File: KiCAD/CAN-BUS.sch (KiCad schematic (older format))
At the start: 11 parts

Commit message: Schematic Rev 0
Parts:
- C16, C18: renamed from C?; value TBD -> 22pF
- gave numbers to parts that had none: 9
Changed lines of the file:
@@
 LIBS:mcp2551
 LIBS:cesd5v0ap
+LIBS:usb_micro_b
 LIBS:Pressure Scanner Board-cache
 EELAYER 25 0
@@
 CAN Controller + Transceiver
 $Comp
-L MCP2515 U?
+L MCP2515 U14
 U 1 1 5C6487A3
 P 4150 3800
-F 0 "U?" H 4150 3175 49  0000 C CNN
+F 0 "U14" H 4150 3175 49  0000 C CNN
 F 1 "MCP2515" H 4150 4500 49  0000 C CNN
 F 2 "" H 2950 3675 49  0001 C CNN
@@
 $EndComp
 $Comp
-L MCP2551 U?
+L MCP2551 U13
 U 1 1 5C6487CB
 P 7600 3775
-F 0 "U?" H 7600 3450 49  0000 C CNN
+F 0 "U13" H 7600 3450 49  0000 C CNN
 F 1 "MCP2551" H 7600 4100 49  0000 C CNN
 F 2 "" H 7600 3775 49  0001 C CNN
@@
 RXCAN
 $Comp
-L GND #PWR?
+L GND #PWR62
 U 1 1 5C648816
 P 3425 4350
-F 0 "#PWR?" H 3425 4100 50  0001 C CNN
+F 0 "#PWR62" H 3425 4100 50  0001 C CNN
 F 1 "GND" H 3425 4200 50  0000 C CNN
 F 2 "" H 3425 4350 50  0001 C CNN
@@
 	3425 4275 3550 4275
 $Comp
-L +3.3V #PWR?
+L +3.3V #PWR55
 U 1 1 5C6489C6
 P 4875 2900
-F 0 "#PWR?" H 4875 2750 50  0001 C CNN
+F 0 "#PWR55" H 4875 2750 50  0001 C CNN
 F 1 "+3.3V" H 4875 3040 50  0000 C CNN
 F 2 "" H 4875 2900 50  0001 C CNN
@@
 NoConn ~ 4750 4275
 $Comp
-L R_Small R?
+L R_Small R10
 U 1 1 5C648A47
 P 5050 3125
-F 0 "R?" H 5080 3145 50  0000 L CNN
+F 0 "R10" H 5080 3145 50  0000 L CNN
 F 1 "10K" H 5080 3085 50  0000 L CNN
 F 2 "" H 5050 3125 50  0001 C CNN
@@
 	5050 4025 4750 4025
 $Comp
-L Crystal Y?
+L Crystal Y2
 U 1 1 5C648B55
 P 2850 4100
-F 0 "Y?" V 2900 4275 50  0000 C CNN
+F 0 "Y2" V 2900 4275 50  0000 C CNN
 F 1 "16MHz" V 2850 3850 50  0000 C CNN
 F 2 "" H 2850 4100 50  0001 C CNN
@@
 	3150 4150 3550 4150
 $Comp
-L C_Small C?
+L C_Small C16
 U 1 1 5C648C45
 P 2325 3900
-F 0 "C?" H 2335 3970 50  0000 L CNN
-F 1 "TBD" H 2335 3820 50  0000 L CNN
+F 0 "C16" V 2425 3925 50  0000 L CNN
+F 1 "22pF" V 2200 3825 50  0000 L CNN
 F 2 "" H 2325 3900 50  0001 C CNN
 F 3 "" H 2325 3900 50  0001 C CNN
@@
 $EndComp
 $Comp
-L C_Small C?
+L C_Small C18
 U 1 1 5C648C82
 P 2325 4300
-F 0 "C?" H 2335 4370 50  0000 L CNN
-F 1 "TBD" H 2335 4220 50  0000 L CNN
+F 0 "C18" V 2200 4200 50  0000 L CNN
+F 1 "22pF" V 2425 4200 50  0000 L CNN
 F 2 "" H 2325 4300 50  0001 C CNN
 F 3 "" H 2325 4300 50  0001 C CNN
@@
 $EndComp
 $Comp
-L GND #PWR?
+L GND #PWR60
 U 1 1 5C648CB1
 P 2050 4100
-F 0 "#PWR?" H 2050 3850 50  0001 C CNN
+F 0 "#PWR60" H 2050 3850 50  0001 C CNN
 F 1 "GND" H 2050 3950 50  0000 C CNN
 F 2 "" H 2050 4100 50  0001 C CNN
@@
 	6975 3575 7125 3575
 $Comp
-L GND #PWR?
+L GND #PWR59
 U 1 1 5C649298
 P 6975 3700
-F 0 "#PWR?" H 6975 3450 50  0001 C CNN
+F 0 "#PWR59" H 6975 3450 50  0001 C CNN
 F 1 "GND" H 6975 3550 50  0000 C CNN
 F 2 "" H 6975 3700 50  0001 C CNN
@@
 	6975 3700 7125 3700
 $Comp
-L +5V #PWR?
+L +5V #PWR58
 U 1 1 5C6492E1
 P 6500 3675
-F 0 "#PWR?" H 6500 3525 50  0001 C CNN
+F 0 "#PWR58" H 6500 3525 50  0001 C CNN
 F 1 "+5V" H 6500 3815 50  0000 C CNN
 F 2 "" H 6500 3675 50  0001 C CNN
@@
 	6500 3825 7125 3825
 $Comp
-L R_Small R?
+L R_Small R11
 U 1 1 5C64939D
 P 8250 3575
-F 0 "R?" V 8400 3550 50  0000 L CNN
+F 0 "R11" V 8400 3550 50  0000 L CNN
 F 1 "17K" V 8325 3500 50  0000 L CNN
 F 2 "" H 8250 3575 50  0001 C CNN
@@
 $EndComp
 $Comp
-L GND #PWR?
+L GND #PWR57
 U 1 1 5C649485
 P 8450 3575
-F 0 "#PWR?" H 8450 3325 50  0001 C CNN
+F 0 "#PWR57" H 8450 3325 50  0001 C CNN
 F 1 "GND" H 8450 3425 50  0000 C CNN
 F 2 "" H 8450 3575 50  0001 C CNN
@@
 NoConn ~ 8075 3950
 $Comp
-L CESD5V0AP D?
+L CESD5V0AP D5
 U 1 1 5C649B06
 P 8400 4275
-F 0 "D?" H 8600 4335 39  0000 C CNN
+F 0 "D5" H 8600 4335 39  0000 C CNN
 F 1 "CESD5V0AP" H 8725 4390 39  0000 C CNN
 F 2 "" H 8400 4275 39  0001 C CNN
@@
 $EndComp
 $Comp
-L GND #PWR?
+L GND #PWR63
 U 1 1 5C649B47
 P 8400 4550
-F 0 "#PWR?" H 8400 4300 50  0001 C CNN
+F 0 "#PWR63" H 8400 4300 50  0001 C CNN
 F 1 "GND" H 8400 4400 50  0000 C CNN
 F 2 "" H 8400 4550 50  0001 C CNN
@@
 	8480 3700 8075 3700
 $Comp
-L R R?
+L R R12
 U 1 1 5C649D1F
 P 9175 3750
-F 0 "R?" V 9255 3750 50  0000 C CNN
+F 0 "R12" V 9255 3750 50  0000 C CNN
 F 1 "120" V 9175 3750 50  0000 C CNN
 F 2 "" V 9105 3750 50  0001 C CNN
@@
 Transient Voltage Protection
 $Comp
-L C_Small C?
+L C_Small C17
 U 1 1 5C64AAF4
 P 6500 3975
-F 0 "C?" H 6400 4050 50  0000 L CNN
+F 0 "C17" H 6400 4050 50  0000 L CNN
 F 1 "100nF" H 6250 3900 50  0000 L CNN
 F 2 "" H 6500 3975 50  0001 C CNN
@@
 $EndComp
 $Comp
-L GND #PWR?
+L GND #PWR61
 U 1 1 5C64ABB3
 P 6500 4125
-F 0 "#PWR?" H 6500 3875 50  0001 C CNN
+F 0 "#PWR61" H 6500 3875 50  0001 C CNN
 F 1 "GND" H 6500 3975 50  0000 C CNN
 F 2 "" H 6500 4125 50  0001 C CNN
@@
 Connection ~ 6500 3825
 $Comp
-L C_Small C?
+L C_Small C15
 U 1 1 5C64AE69
 P 5300 3125
-F 0 "C?" H 5310 3195 50  0000 L CNN
+F 0 "C15" H 5310 3195 50  0000 L CNN
 F 1 "100nF" H 5310 3045 50  0000 L CNN
 F 2 "" H 5300 3125 50  0001 C CNN
@@
 Connection ~ 5050 2950
 $Comp
-L GND #PWR?
+L GND #PWR56
 U 1 1 5C64B180
 P 5300 3275
-F 0 "#PWR?" H 5300 3025 50  0001 C CNN
+F 0 "#PWR56" H 5300 3025 50  0001 C CNN
 F 1 "GND" H 5300 3125 50  0000 C CNN
 F 2 "" H 5300 3275 50  0001 C CNN

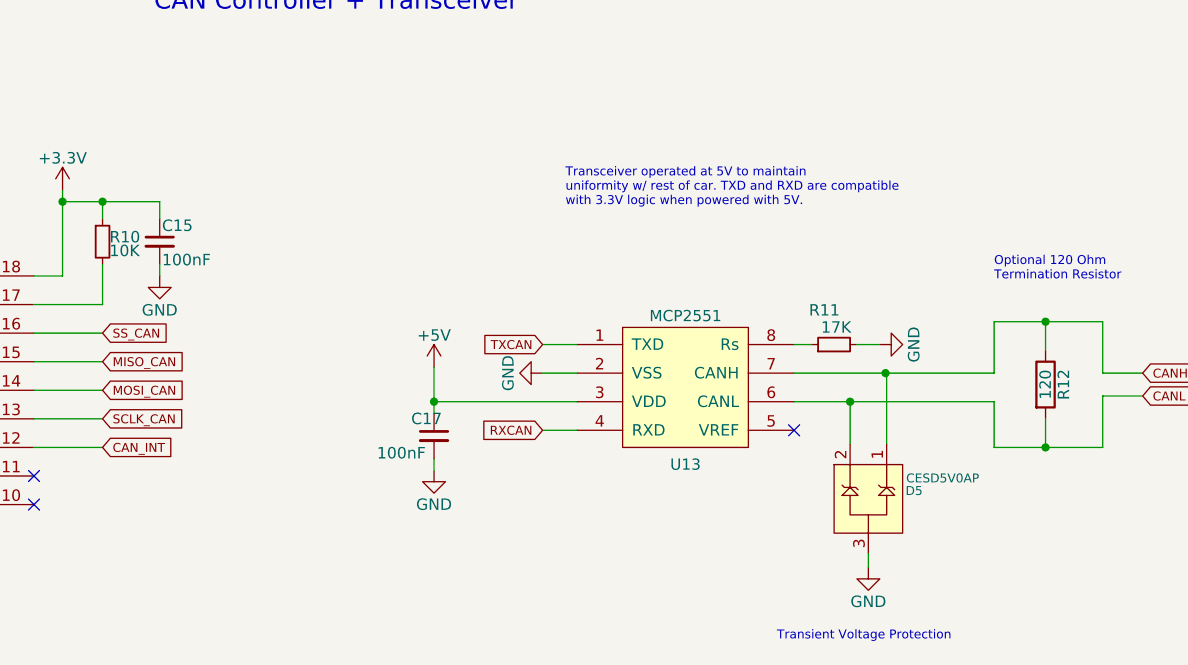
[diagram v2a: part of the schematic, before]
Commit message: Added footprints for all components and created BOM
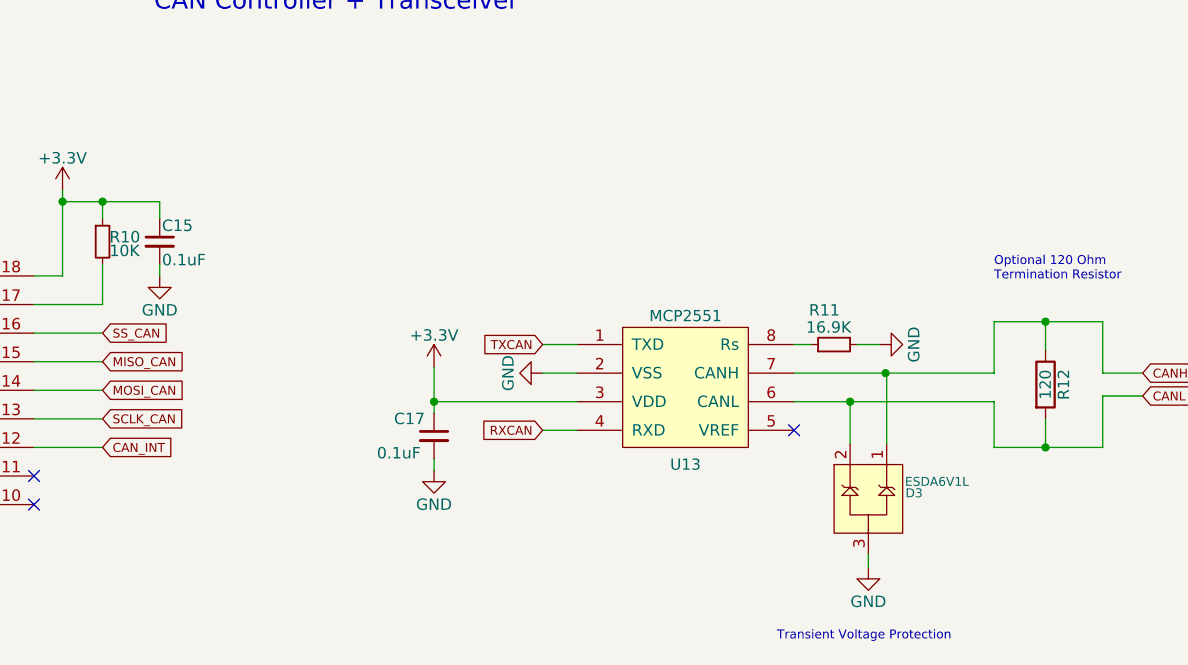
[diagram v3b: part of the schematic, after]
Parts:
- removed D5: CESD5V0AP, symbol CESD5V0AP
- added D3: ESDA6V1L, TO_SOT_Packages_SMD:SOT-23, symbol ESDA6V1L
- C15, C17: value 100nF -> 0.1uF; footprint (none) -> Capacitors_SMD:C_1206
- C16, C18: footprint (none) -> Capacitors_SMD:C_0805
- R10: footprint (none) -> Resistors_SMD:R_1210
- R11: value 17K -> 16.9K; footprint (none) -> Resistors_SMD:R_0805
- R12: footprint (none) -> Resistors_SMD:R_0805
- U13: footprint (none) -> Housings_SOIC:SOIC-8-1EP_3.9x4.9mm_Pitch1.27mm
- U14: footprint (none) -> Housings_SOIC:SOIC-18W_7.5x11.6mm_Pitch1.27mm
- Y2: footprint (none) -> 9B-16.000MEEJ-B:9B-16.000MEEJ-B
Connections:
- net +5V is gone; now on net +3V3: C17.1, U13.3 (VDD)
- net CANH: now also D3.1
- net CANL: now also D3.2
- net GND: now also D3.3
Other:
- note removed: "Transceiver operated at 5V to maintain\nuniformity w/ rest of car. TXD and RXD are compatible\nwith 3.3V logic when powered with 5V."
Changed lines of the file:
@@
 F 0 "U14" H 4150 3175 49  0000 C CNN
 F 1 "MCP2515" H 4150 4500 49  0000 C CNN
-F 2 "" H 2950 3675 49  0001 C CNN
+F 2 "Housings_SOIC:SOIC-18W_7.5x11.6mm_Pitch1.27mm" H 2950 3675 49  0001 C CNN
 F 3 "" H 2950 3675 49  0001 C CNN
 	1    4150 3800
@@
 F 0 "U13" H 7600 3450 49  0000 C CNN
 F 1 "MCP2551" H 7600 4100 49  0000 C CNN
-F 2 "" H 7600 3775 49  0001 C CNN
+F 2 "Housings_SOIC:SOIC-8-1EP_3.9x4.9mm_Pitch1.27mm" H 7600 3775 49  0001 C CNN
 F 3 "" H 7600 3775 49  0001 C CNN
 	1    7600 3775
@@
 RXCAN
 $Comp
-L GND #PWR055
+L GND #PWR053
 U 1 1 5C648816
 P 3425 4350
-F 0 "#PWR055" H 3425 4100 50  0001 C CNN
+F 0 "#PWR053" H 3425 4100 50  0001 C CNN
 F 1 "GND" H 3425 4200 50  0000 C CNN
 F 2 "" H 3425 4350 50  0001 C CNN
@@
 	3425 4275 3550 4275
 $Comp
-L +3.3V #PWR056
+L +3.3V #PWR054
 U 1 1 5C6489C6
 P 4875 2900
-F 0 "#PWR056" H 4875 2750 50  0001 C CNN
+F 0 "#PWR054" H 4875 2750 50  0001 C CNN
 F 1 "+3.3V" H 4875 3040 50  0000 C CNN
 F 2 "" H 4875 2900 50  0001 C CNN
@@
 F 0 "R10" H 5080 3145 50  0000 L CNN
 F 1 "10K" H 5080 3085 50  0000 L CNN
-F 2 "" H 5050 3125 50  0001 C CNN
+F 2 "Resistors_SMD:R_1210" H 5050 3125 50  0001 C CNN
 F 3 "" H 5050 3125 50  0001 C CNN
 	1    5050 3125
@@
 F 0 "Y2" V 2900 4275 50  0000 C CNN
 F 1 "16MHz" V 2850 3850 50  0000 C CNN
-F 2 "" H 2850 4100 50  0001 C CNN
+F 2 "9B-16.000MEEJ-B:9B-16.000MEEJ-B" H 2850 4100 50  0001 C CNN
 F 3 "" H 2850 4100 50  0001 C CNN
 	1    2850 4100
@@
 F 0 "C16" V 2425 3925 50  0000 L CNN
 F 1 "22pF" V 2200 3825 50  0000 L CNN
-F 2 "" H 2325 3900 50  0001 C CNN
+F 2 "Capacitors_SMD:C_0805" H 2325 3900 50  0001 C CNN
 F 3 "" H 2325 3900 50  0001 C CNN
 	1    2325 3900
@@
 F 0 "C18" V 2200 4200 50  0000 L CNN
 F 1 "22pF" V 2425 4200 50  0000 L CNN
-F 2 "" H 2325 4300 50  0001 C CNN
+F 2 "Capacitors_SMD:C_0805" H 2325 4300 50  0001 C CNN
 F 3 "" H 2325 4300 50  0001 C CNN
 	1    2325 4300
@@
 $EndComp
 $Comp
-L GND #PWR057
+L GND #PWR055
 U 1 1 5C648CB1
 P 2050 4100
-F 0 "#PWR057" H 2050 3850 50  0001 C CNN
+F 0 "#PWR055" H 2050 3850 50  0001 C CNN
 F 1 "GND" H 2050 3950 50  0000 C CNN
 F 2 "" H 2050 4100 50  0001 C CNN
@@
 	2150 4300 2225 4300
 Connection ~ 2150 4100
-Text Notes 7075 2975 0    39   ~ 0
-Transceiver operated at 5V to maintain\nuniformity w/ rest of car. TXD and RXD are compatible\nwith 3.3V logic when powered with 5V.
 Text GLabel 6975 3575 0    39   Input ~ 0
 TXCAN
@@
 	6975 3575 7125 3575
 $Comp
-L GND #PWR058
+L GND #PWR056
 U 1 1 5C649298
 P 6975 3700
-F 0 "#PWR058" H 6975 3450 50  0001 C CNN
+F 0 "#PWR056" H 6975 3450 50  0001 C CNN
 F 1 "GND" H 6975 3550 50  0000 C CNN
 F 2 "" H 6975 3700 50  0001 C CNN
@@
 Wire Wire Line
 	6975 3700 7125 3700
-$Comp
-L +5V #PWR059
-U 1 1 5C6492E1
-P 6500 3675
-F 0 "#PWR059" H 6500 3525 50  0001 C CNN
-F 1 "+5V" H 6500 3815 50  0000 C CNN
-F 2 "" H 6500 3675 50  0001 C CNN
-F 3 "" H 6500 3675 50  0001 C CNN
-	1    6500 3675
-	1    0    0    -1
-$EndComp
 Wire Wire Line
 	6500 3675 6500 3875
@@
 P 8250 3575
 F 0 "R11" V 8400 3550 50  0000 L CNN
-F 1 "17K" V 8325 3500 50  0000 L CNN
-F 2 "" H 8250 3575 50  0001 C CNN
+F 1 "16.9K" V 8325 3500 50  0000 L CNN
+F 2 "Resistors_SMD:R_0805" H 8250 3575 50  0001 C CNN
 F 3 "" H 8250 3575 50  0001 C CNN
 	1    8250 3575
@@
 $EndComp
 $Comp
-L GND #PWR060
+L GND #PWR057
 U 1 1 5C649485
 P 8450 3575
-F 0 "#PWR060" H 8450 3325 50  0001 C CNN
+F 0 "#PWR057" H 8450 3325 50  0001 C CNN
 F 1 "GND" H 8450 3425 50  0000 C CNN
 F 2 "" H 8450 3575 50  0001 C CNN
@@
 NoConn ~ 8075 3950
 $Comp
-L CESD5V0AP D5
-U 1 1 5C649B06
-P 8400 4275
-F 0 "D5" H 8600 4335 39  0000 C CNN
-F 1 "CESD5V0AP" H 8725 4390 39  0000 C CNN
-F 2 "" H 8400 4275 39  0001 C CNN
-F 3 "" H 8400 4275 39  0001 C CNN
-	1    8400 4275
-	1    0    0    -1
-$EndComp
-$Comp
-L GND #PWR061
+L GND #PWR058
 U 1 1 5C649B47
 P 8400 4550
-F 0 "#PWR061" H 8400 4300 50  0001 C CNN
+F 0 "#PWR058" H 8400 4300 50  0001 C CNN
 F 1 "GND" H 8400 4400 50  0000 C CNN
 F 2 "" H 8400 4550 50  0001 C CNN
@@
 F 0 "R12" V 9255 3750 50  0000 C CNN
 F 1 "120" V 9175 3750 50  0000 C CNN
-F 2 "" V 9105 3750 50  0001 C CNN
+F 2 "Resistors_SMD:R_0805" V 9105 3750 50  0001 C CNN
 F 3 "" H 9175 3750 50  0001 C CNN
 	1    9175 3750
@@
 U 1 1 5C64AAF4
 P 6500 3975
-F 0 "C17" H 6400 4050 50  0000 L CNN
-F 1 "100nF" H 6250 3900 50  0000 L CNN
-F 2 "" H 6500 3975 50  0001 C CNN
+F 0 "C17" H 6325 4050 50  0000 L CNN
+F 1 "0.1uF" H 6250 3900 50  0000 L CNN
+F 2 "Capacitors_SMD:C_1206" H 6500 3975 50  0001 C CNN
 F 3 "" H 6500 3975 50  0001 C CNN
 	1    6500 3975
@@
 $EndComp
 $Comp
-L GND #PWR062
+L GND #PWR059
 U 1 1 5C64ABB3
 P 6500 4125
-F 0 "#PWR062" H 6500 3875 50  0001 C CNN
+F 0 "#PWR059" H 6500 3875 50  0001 C CNN
 F 1 "GND" H 6500 3975 50  0000 C CNN
 F 2 "" H 6500 4125 50  0001 C CNN
@@
 P 5300 3125
 F 0 "C15" H 5310 3195 50  0000 L CNN
-F 1 "100nF" H 5310 3045 50  0000 L CNN
-F 2 "" H 5300 3125 50  0001 C CNN
+F 1 "0.1uF" H 5310 3045 50  0000 L CNN
+F 2 "Capacitors_SMD:C_1206" H 5300 3125 50  0001 C CNN
 F 3 "" H 5300 3125 50  0001 C CNN
 	1    5300 3125
@@
 Connection ~ 5050 2950
 $Comp
-L GND #PWR063
+L GND #PWR060
 U 1 1 5C64B180
 P 5300 3275
-F 0 "#PWR063" H 5300 3025 50  0001 C CNN
+F 0 "#PWR060" H 5300 3025 50  0001 C CNN
 F 1 "GND" H 5300 3125 50  0000 C CNN
 F 2 "" H 5300 3275 50  0001 C CNN
@@
 Wire Wire Line
 	5300 3275 5300 3225
+$Comp
+L +3.3V #PWR061
+U 1 1 5C86C257
+P 6500 3675
+F 0 "#PWR061" H 6500 3525 50  0001 C CNN
+F 1 "+3.3V" H 6500 3815 50  0000 C CNN
+F 2 "" H 6500 3675 50  0001 C CNN
+F 3 "" H 6500 3675 50  0001 C CNN
+	1    6500 3675
+	1    0    0    -1
+$EndComp
+$Comp
+L ESDA6V1L D3
+U 1 1 5C86D38B
+P 8400 4275
+F 0 "D3" H 8600 4325 39  0000 C CNN
+F 1 "ESDA6V1L" H 8700 4375 39  0000 C CNN
+F 2 "TO_SOT_Packages_SMD:SOT-23" H 8400 4275 39  0001 C CNN
+F 3 "" H 8400 4275 39  0001 C CNN
+	1    8400 4275
+	1    0    0    -1
+$EndComp
 $EndSCHEMATC

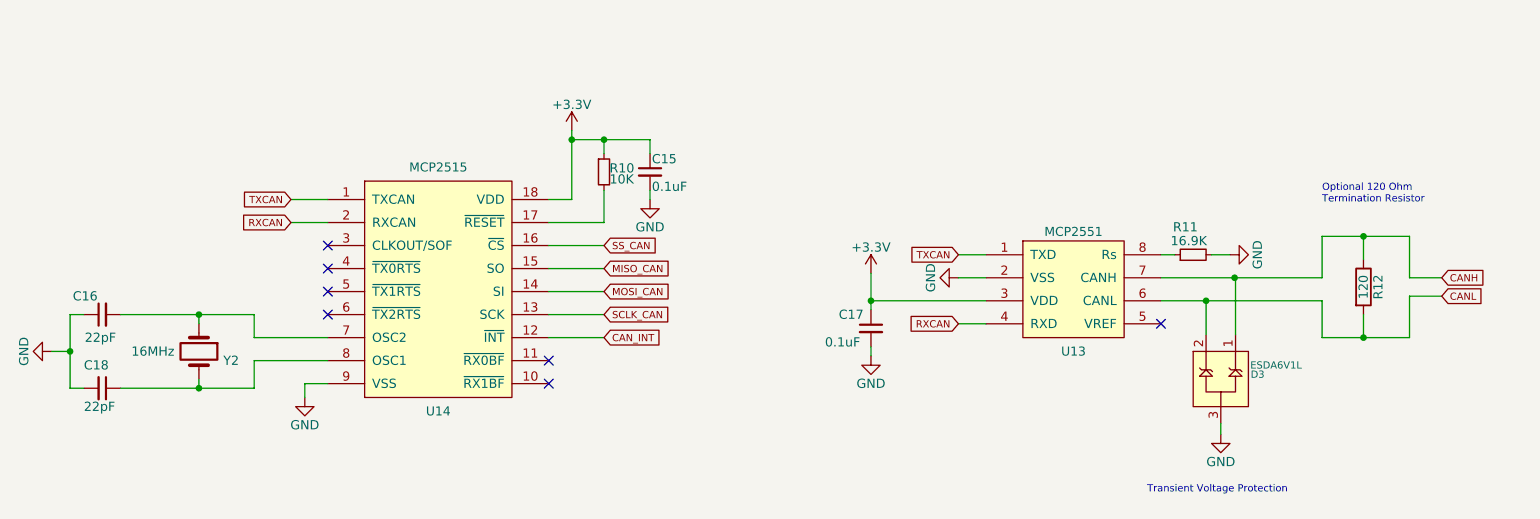
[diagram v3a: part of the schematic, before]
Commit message: Corrected schematic error, began layout.
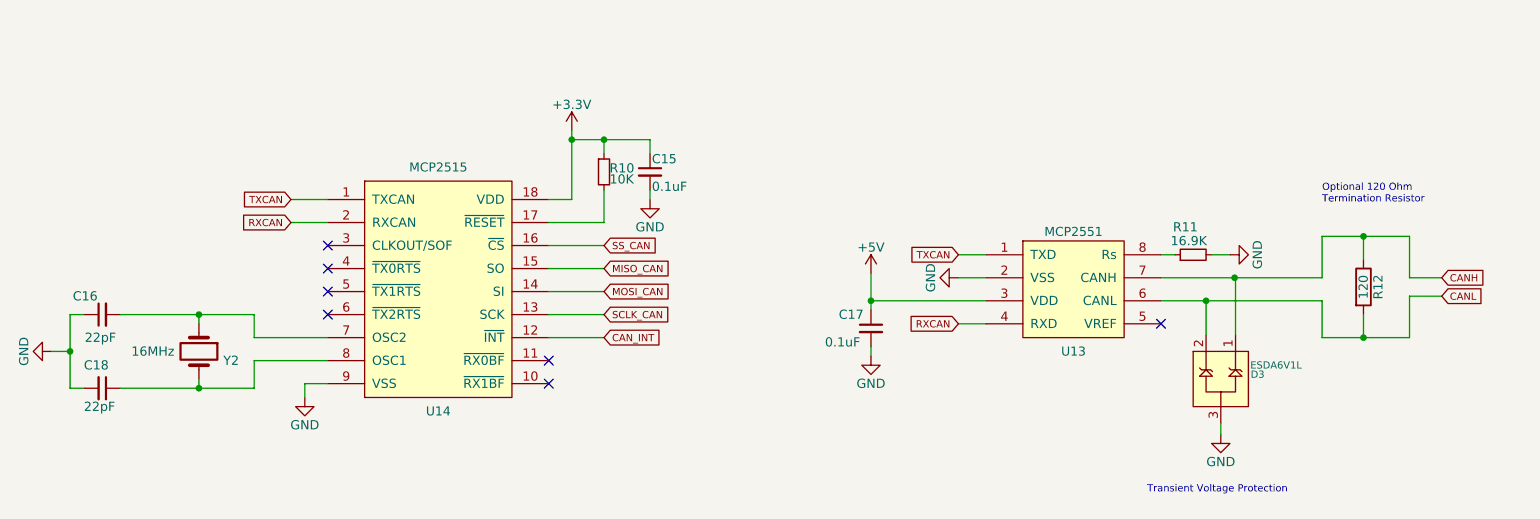
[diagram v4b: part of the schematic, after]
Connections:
- net +3V3: no longer C17.1, U13.3 (VDD)
- new net +5V: C17.1, U13.3 (VDD)
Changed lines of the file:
@@
 	3150 4025 3150 3900
 Wire Wire Line
-	3150 3900 2425 3900
+	3150 3900 2850 3900
+Wire Wire Line
+	2850 3900 2425 3900
 Wire Wire Line
 	2850 3900 2850 3950
@@
 	2850 4250 2850 4300
 Wire Wire Line
-	2425 4300 3150 4300
+	2425 4300 2850 4300
+Wire Wire Line
+	2850 4300 3150 4300
 Wire Wire Line
 	3150 4300 3150 4150
@@
 	2050 4100 2150 4100
 Wire Wire Line
-	2150 3900 2150 4300
+	2150 3900 2150 4100
+Wire Wire Line
+	2150 4100 2150 4300
 Wire Wire Line
 	2150 3900 2225 3900
@@
 	6975 3700 7125 3700
 Wire Wire Line
-	6500 3675 6500 3875
+	6500 3675 6500 3825
+Wire Wire Line
+	6500 3825 6500 3875
 Wire Wire Line
 	6500 3825 7125 3825
@@
 	8320 4010 8320 3825
 Wire Wire Line
-	8075 3825 8950 3825
+	8075 3825 8320 3825
+Wire Wire Line
+	8320 3825 8950 3825
 Wire Wire Line
 	8480 4010 8480 3700
 Wire Wire Line
-	8480 3700 8075 3700
+	8480 3700 8475 3700
+Wire Wire Line
+	8475 3700 8075 3700
 $Comp
 L R R12
@@
 	8950 3700 8950 3475
 Wire Wire Line
-	8950 3475 9425 3475
+	8950 3475 9175 3475
+Wire Wire Line
+	9175 3475 9425 3475
 Wire Wire Line
 	9175 3475 9175 3600
@@
 	9175 3900 9175 4025
 Wire Wire Line
-	8950 4025 9425 4025
+	8950 4025 9175 4025
+Wire Wire Line
+	9175 4025 9425 4025
 Wire Wire Line
 	8950 3825 8950 4025
@@
 $EndComp
 Wire Wire Line
-	4875 2900 4875 3275
+	4875 2900 4875 2950
+Wire Wire Line
+	4875 2950 4875 3275
 Wire Wire Line
 	4875 3275 4750 3275
 Wire Wire Line
-	4875 2950 5300 2950
+	4875 2950 5050 2950
+Wire Wire Line
+	5050 2950 5300 2950
 Wire Wire Line
 	5050 2950 5050 3025
@@
 	5300 3275 5300 3225
 $Comp
-L +3.3V #PWR061
-U 1 1 5C86C257
-P 6500 3675
-F 0 "#PWR061" H 6500 3525 50  0001 C CNN
-F 1 "+3.3V" H 6500 3815 50  0000 C CNN
-F 2 "" H 6500 3675 50  0001 C CNN
-F 3 "" H 6500 3675 50  0001 C CNN
-	1    6500 3675
-	1    0    0    -1
-$EndComp
-$Comp
 L ESDA6V1L D3
 U 1 1 5C86D38B
@@
 	1    0    0    -1
 $EndComp
+$Comp
+L +5V #PWR?
+U 1 1 5C8EBD26
+P 6500 3675
+F 0 "#PWR?" H 6500 3525 50  0001 C CNN
+F 1 "+5V" H 6500 3815 50  0000 C CNN
+F 2 "" H 6500 3675 50  0001 C CNN
+F 3 "" H 6500 3675 50  0001 C CNN
+	1    6500 3675
+	1    0    0    -1
+$EndComp
